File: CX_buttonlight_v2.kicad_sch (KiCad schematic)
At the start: 14 parts, among them U1 LM317LIPK

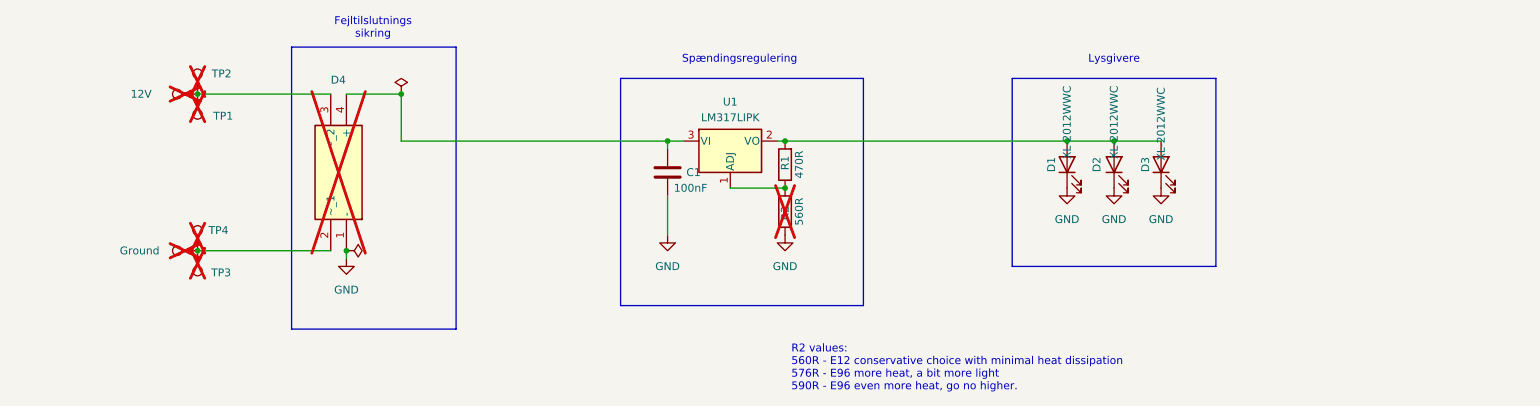
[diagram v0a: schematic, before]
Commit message: Fuse added, minor fix in link given in README.md fixed
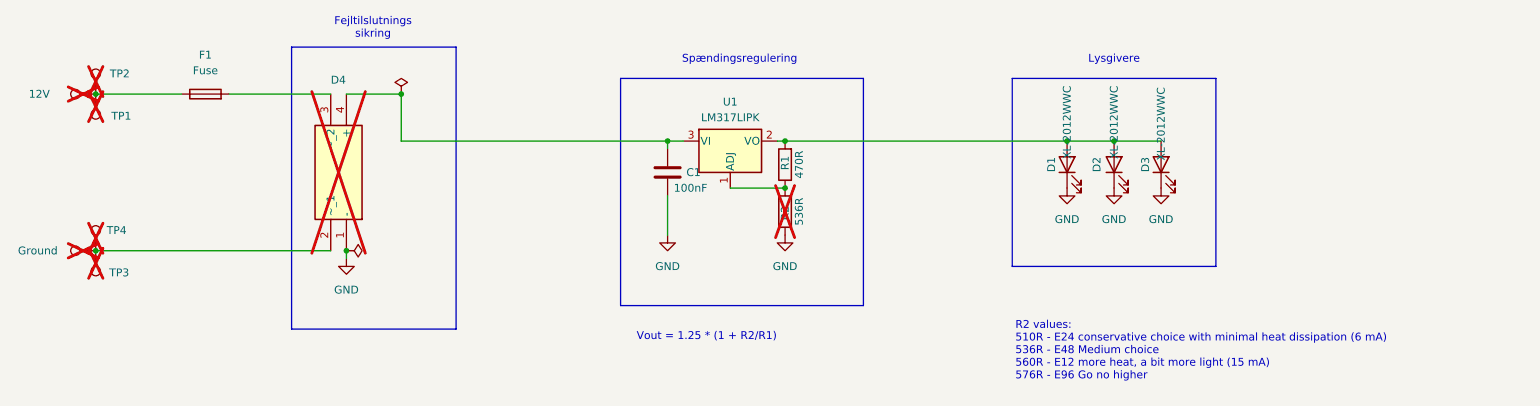
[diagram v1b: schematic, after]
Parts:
- added F1: Fuse, Fuse:Fuse_0805_2012Metric_Pad1.15x1.40mm_HandSolder, symbol Device:Fuse
- R2: value 560R -> 536R
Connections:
- net at Supply1.1, TP1.1, TP2.1: now also F1.1; no longer D4.3 (~_2)
- new net: D4.3 (~_2), F1.2
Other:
- note added: "R2 values: 510R - E24 conservative choice with minimal heat dissipation (6 mA) 536R - E48 Medium choice 560R - E12 more heat, a bit more light (15 mA) 576R - E96 Go no higher"
- note added: "Vout = 1.25 * (1 + R2/R1)"
- note removed: "R2 values: 560R - E12 conservative choice with minimal heat dissipation 576R - E96 more heat, a bit more light 590R - E96 even more heat, go no higher."
- moved on the sheet: TP1, TP2, TP3, TP4
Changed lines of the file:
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@@
 	)
 	(junction
-		(at 55.88 69.85)
+		(at 39.37 69.85)
 		(diameter 0)
 		(color 0 0 0 0)
 	)
 	(junction
-		(at 55.88 95.25)
+		(at 39.37 95.25)
 		(diameter 0)
 		(color 0 0 0 0)
@@
 	(wire
 		(pts
-			(xy 55.88 69.85) (xy 77.47 69.85)
+			(xy 39.37 69.85) (xy 53.34 69.85)
 		)
 		(stroke
@@
 	(wire
 		(pts
-			(xy 55.88 95.25) (xy 77.47 95.25)
+			(xy 39.37 95.25) (xy 77.47 95.25)
 		)
 		(stroke
@@
 		(pts
 			(xy 149.86 77.47) (xy 151.13 77.47)
+		)
+		(stroke
+			(width 0)
+			(type default)
+		)
+	)
+	(wire
+		(pts
+			(xy 60.96 69.85) (xy 77.47 69.85)
 		)
 		(stroke
@@
 		)
 	)
-	(text "R2 values:\n560R - E12 conservative choice with minimal heat dissipation\n576R - E96 more heat, a bit more light\n590R - E96 even more heat, go no higher."
+	(text "R2 values:\n510R - E24 conservative choice with minimal heat dissipation (6 mA)\n536R - E48 Medium choice\n560R - E12 more heat, a bit more light (15 mA)\n576R - E96 Go no higher\n"
 		(exclude_from_sim yes)
-		(at 152.146 114.3 0)
+		(at 188.468 111.506 0)
 		(effects
 			(font
@@
 			)
 			(justify left)
+		)
+	)
+	(text "Vout = 1.25 * (1 + R2/R1)"
+		(exclude_from_sim no)
+		(at 138.43 109.22 0)
+		(effects
+			(font
+				(size 1.27 1.27)
+			)
 		)
 	)
@@
 	(symbol
 		(lib_id "Connector:TestPoint")
-		(at 55.88 95.25 180)
+		(at 39.37 95.25 180)
 		(unit 1)
 		(exclude_from_sim no)
@@
 		(dnp yes)
 		(property "Reference" "TP3"
-			(at 59.69 98.806 0)
+			(at 43.18 98.806 0)
 			(effects
 				(font
@@
 		)
 		(property "Value" "TestPoint"
-			(at 52.6381 98.552 90)
+			(at 36.1281 98.552 90)
 			(effects
 				(font
@@
 		)
 		(property "Footprint" "TestPoint:TestPoint_THTPad_D1.5mm_Drill0.7mm"
-			(at 50.8 95.25 0)
+			(at 34.29 95.25 0)
 			(effects
 				(font
@@
 		)
 		(property "Datasheet" "~"
-			(at 50.8 95.25 0)
+			(at 34.29 95.25 0)
 			(effects
 				(font
@@
 		)
 		(property "Description" "test point"
-			(at 55.88 95.25 0)
+			(at 39.37 95.25 0)
 			(effects
 				(font
@@
 		)
 		(property "LCSC Part #" ""
-			(at 55.88 95.25 0)
+			(at 39.37 95.25 0)
 			(effects
 				(font
@@
 	(symbol
 		(lib_id "Connector:TestPoint")
-		(at 55.88 69.85 90)
+		(at 39.37 69.85 90)
 		(unit 1)
 		(exclude_from_sim no)
@@
 		(dnp yes)
 		(property "Reference" "Supply1"
-			(at 51.562 66.04 90)
+			(at 35.052 66.04 90)
 			(effects
 				(font
@@
 		)
 		(property "Value" "12V"
-			(at 46.736 69.85 90)
+			(at 30.226 69.85 90)
 			(effects
 				(font
@@
 		)
 		(property "Footprint" "TestPoint:TestPoint_THTPad_D1.5mm_Drill0.7mm"
-			(at 55.88 64.77 0)
+			(at 39.37 64.77 0)
 			(effects
 				(font
@@
 		)
 		(property "Datasheet" "~"
-			(at 55.88 64.77 0)
+			(at 39.37 64.77 0)
 			(effects
 				(font
@@
 		)
 		(property "Description" "test point"
-			(at 55.88 69.85 0)
+			(at 39.37 69.85 0)
 			(effects
 				(font
@@
 		)
 		(property "Sim.Device" ""
-			(at 55.88 69.85 0)
+			(at 39.37 69.85 0)
 			(effects
 				(font
@@
 		)
 		(property "Sim.Pins" ""
-			(at 55.88 69.85 0)
+			(at 39.37 69.85 0)
 			(effects
 				(font
@@
 		)
 		(property "LCSC Part #" ""
-			(at 55.88 69.85 0)
+			(at 39.37 69.85 0)
 			(effects
 				(font
@@
 	(symbol
 		(lib_id "Connector:TestPoint")
-		(at 55.88 95.25 0)
+		(at 39.37 95.25 0)
 		(unit 1)
 		(exclude_from_sim no)
@@
 		(dnp yes)
 		(property "Reference" "TP4"
-			(at 57.658 91.948 0)
+			(at 41.148 91.948 0)
 			(effects
 				(font
@@
 		)
 		(property "Value" "TestPoint"
-			(at 57.785 93.2179 0)
+			(at 41.275 93.2179 0)
 			(effects
 				(font
@@
 		)
 		(property "Footprint" "TestPoint:TestPoint_THTPad_D1.5mm_Drill0.7mm"
-			(at 60.96 95.25 0)
+			(at 44.45 95.25 0)
 			(effects
 				(font
@@
 		)
 		(property "Datasheet" "~"
-			(at 60.96 95.25 0)
+			(at 44.45 95.25 0)
 			(effects
 				(font
@@
 		)
 		(property "Description" "test point"
-			(at 55.88 95.25 0)
+			(at 39.37 95.25 0)
 			(effects
 				(font
@@
 		)
 		(property "LCSC Part #" ""
-			(at 55.88 95.25 0)
+			(at 39.37 95.25 0)
 			(effects
 				(font
@@
 	(symbol
 		(lib_id "Connector:TestPoint")
-		(at 55.88 69.85 0)
+		(at 39.37 69.85 0)
 		(unit 1)
 		(exclude_from_sim no)
@@
 		(dnp yes)
 		(property "Reference" "TP2"
-			(at 58.166 66.548 0)
+			(at 41.656 66.548 0)
 			(effects
 				(font
@@
 		)
 		(property "Value" "TestPoint"
-			(at 58.42 67.8179 0)
+			(at 41.91 67.8179 0)
 			(effects
 				(font
@@
 		)
 		(property "Footprint" "TestPoint:TestPoint_THTPad_D1.5mm_Drill0.7mm"
-			(at 60.96 69.85 0)
+			(at 44.45 69.85 0)
 			(effects
 				(font
@@
 		)
 		(property "Datasheet" "~"
-			(at 60.96 69.85 0)
+			(at 44.45 69.85 0)
 			(effects
 				(font
@@
 		)
 		(property "Description" "test point"
-			(at 55.88 69.85 0)
+			(at 39.37 69.85 0)
 			(effects
 				(font
@@
 		)
 		(property "LCSC Part #" ""
-			(at 55.88 69.85 0)
+			(at 39.37 69.85 0)
 			(effects
 				(font
@@
 	(symbol
 		(lib_id "Connector:TestPoint")
-		(at 55.88 69.85 180)
+		(at 39.37 69.85 180)
 		(unit 1)
 		(exclude_from_sim no)
@@
 		(dnp yes)
 		(property "Reference" "TP1"
-			(at 58.42 73.406 0)
+			(at 41.91 73.406 0)
 			(effects
 				(font
@@
 		)
 		(property "Value" "TestPoint"
-			(at 58.42 74.4219 0)
+			(at 41.91 74.4219 0)
 			(effects
 				(font
@@
 		)
 		(property "Footprint" "TestPoint:TestPoint_THTPad_D1.5mm_Drill0.7mm"
-			(at 50.8 69.85 0)
+			(at 34.29 69.85 0)
 			(effects
 				(font
@@
 		)
 		(property "Datasheet" "~"
-			(at 50.8 69.85 0)
+			(at 34.29 69.85 0)
 			(effects
 				(font
@@
 		)
 		(property "Description" "test point"
-			(at 55.88 69.85 0)
+			(at 39.37 69.85 0)
 			(effects
 				(font
@@
 		)
 		(property "LCSC Part #" ""
-			(at 55.88 69.85 0)
+			(at 39.37 69.85 0)
 			(effects
 				(font
@@
 	(symbol
 		(lib_id "Connector:TestPoint")
-		(at 55.88 95.25 90)
+		(at 39.37 95.25 90)
 		(unit 1)
 		(exclude_from_sim no)
@@
 		(dnp yes)
 		(property "Reference" "Ground1"
-			(at 58.42 95.25 90)
+			(at 41.91 95.25 90)
 			(effects
 				(font
@@
 		)
 		(property "Value" "Ground"
-			(at 46.482 95.25 90)
+			(at 29.972 95.25 90)
 			(effects
 				(font
@@
 		)
 		(property "Footprint" "TestPoint:TestPoint_THTPad_D1.5mm_Drill0.7mm"
-			(at 55.88 90.17 0)
+			(at 39.37 90.17 0)
 			(effects
 				(font
@@
 		)
 		(property "Datasheet" "~"
-			(at 55.88 90.17 0)
+			(at 39.37 90.17 0)
 			(effects
 				(font
@@
 		)
 		(property "Description" "test point"
-			(at 55.88 95.25 0)
+			(at 39.37 95.25 0)
 			(effects
 				(font
@@
 		)
 		(property "Sim.Device" ""
-			(at 55.88 95.25 0)
+			(at 39.37 95.25 0)
 			(effects
 				(font
@@
 		)
 		(property "Sim.Pins" ""
-			(at 55.88 95.25 0)
+			(at 39.37 95.25 0)
 			(effects
 				(font
@@
 		)
 		(property "LCSC Part #" ""
-			(at 55.88 95.25 0)
+			(at 39.37 95.25 0)
 			(effects
 				(font
@@
 			)
 		)
-		(property "Value" "560R"
+		(property "Value" "536R"
 			(at 153.416 88.9 90)
 			(effects
@@
 					(unit 1)
 				)
+			)
+		)
+	)
+	(symbol
+		(lib_id "Device:Fuse")
+		(at 57.15 69.85 90)
+		(unit 1)
+		(exclude_from_sim no)
+		(in_bom yes)
+		(on_board yes)
+		(dnp no)
+		(fields_autoplaced yes)
+		(property "Reference" "F1"
+			(at 57.15 63.5 90)
+			(effects
+				(font
+					(size 1.27 1.27)
+				)
+			)
+		)
+		(property "Value" "Fuse"
+			(at 57.15 66.04 90)
+			(effects
+				(font
+					(size 1.27 1.27)
+				)
+			)
+		)
+		(property "Footprint" "Fuse:Fuse_0805_2012Metric_Pad1.15x1.40mm_HandSolder"
+			(at 57.15 71.628 90)
+			(effects
+				(font
+					(size 1.27 1.27)
+				)
+				(hide yes)
+			)
+		)
+		(property "Datasheet" "~"
+			(at 57.15 69.85 0)
+			(effects
+				(font
+					(size 1.27 1.27)
+				)
+				(hide yes)
+			)
+		)
+		(property "Description" "Fuse"
+			(at 57.15 69.85 0)
+			(effects
+				(font
+					(size 1.27 1.27)
+				)
+				(hide yes)
+			)
+		)
+		(pin "1"
+		)
+		(pin "2"
+		)
+		(instances
+			(project "CX_buttonlight_v2"
+				(path "/a6c7f972-13d1-471d-8078-ec61320b86a9"
+					(reference "F1")
+					(unit 1)
+				)
